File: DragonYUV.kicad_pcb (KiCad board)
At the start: 4 copper layers, 120 x 45.6 mm, 72 parts, among them IC1 74HCT273, IC11 74LS123N, IC2 MC6847, J1 Video Output, J2 Board Interconnect Male, J3 JTAG, J4 SVid, Q1 MMBT4401, Q2 NPN, Q3 NPN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

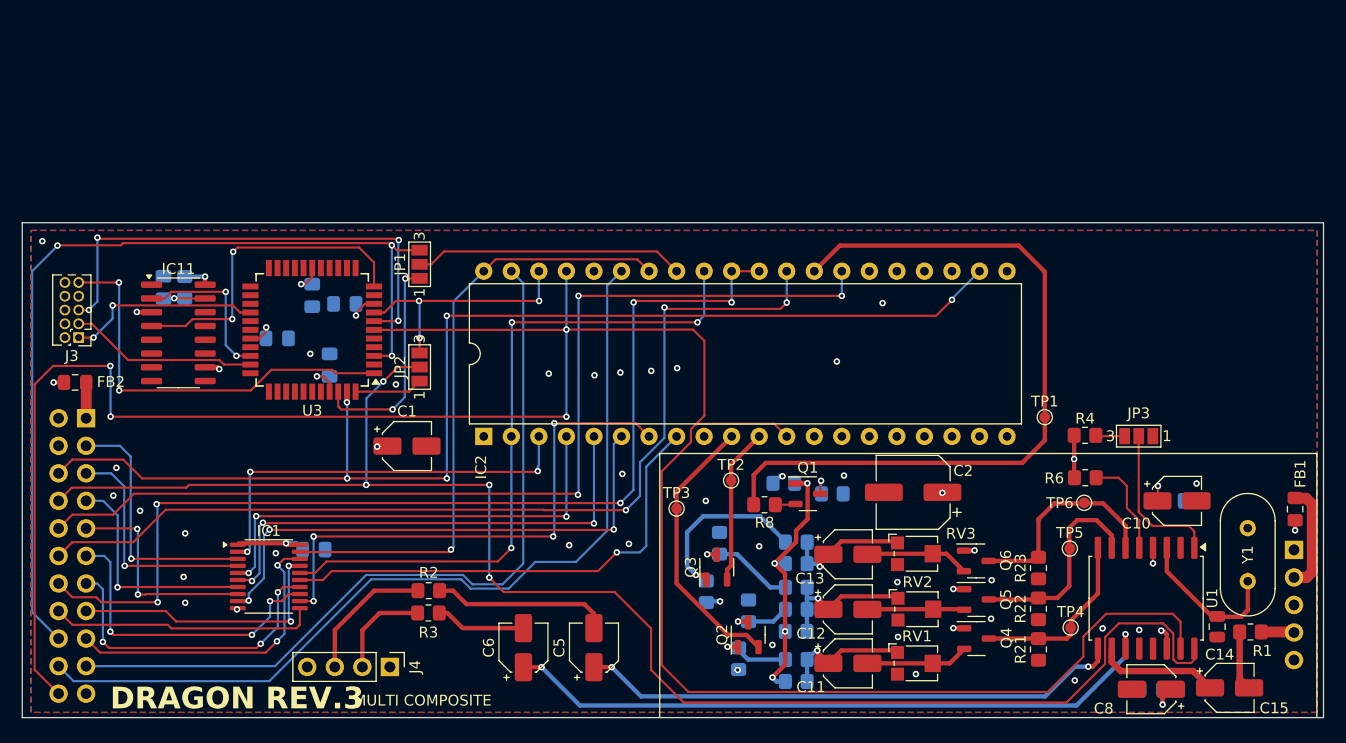
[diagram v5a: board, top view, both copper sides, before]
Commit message: rework schematics for demux of video
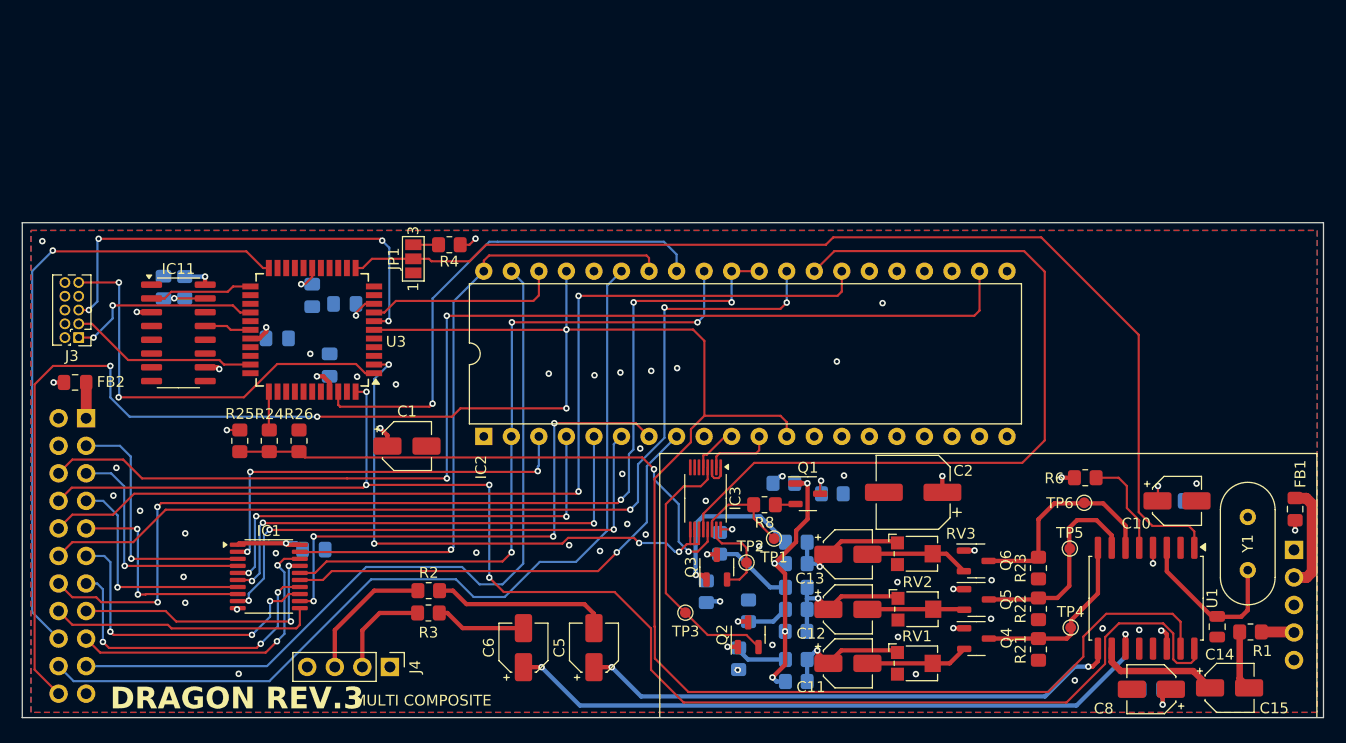
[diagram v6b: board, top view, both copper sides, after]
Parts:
- removed JP2: Video HS, Jumper:SolderJumper-3_P1.3mm_Open_Pad1.0x1.5mm_NumberLabels
- removed JP3: Video Format, Jumper:SolderJumper-3_P1.3mm_Open_Pad1.0x1.5mm_NumberLabels
- added IC3: MC14053, Package_SO:TSSOP-16_4.4x3.6mm_P0.4mm, F.Cu at (153.0, 106.9)
- added R24: 12K, Resistor_SMD:R_0805_2012Metric_Pad1.20x1.40mm_HandSolder, F.Cu at (112.8, 101.6)
- added R25: 8K2, Resistor_SMD:R_0805_2012Metric_Pad1.20x1.40mm_HandSolder, F.Cu at (110.1, 101.6)
- added R26: 1K8, Resistor_SMD:R_0805_2012Metric_Pad1.20x1.40mm_HandSolder, F.Cu at (115.5, 101.6)
- JP1: value Video Clock -> Video Format
- moved R4 61.2 mm to (129.4, 83.5), turned to 0 degrees
- moved TP1 27.4 mm to (159.4, 110.6)
- moved TP3 9.64 mm to (151.2, 117.4)
- moved TP2 7.70 mm to (156.8, 112.8)
- moved Y1 1.03 mm to (203.0, 108.6)
- moved JP1 0.77 mm to (126.1, 84.8)
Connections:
- IC11 pad 13: unconnected-(IC11A-Q-Pad13) -> SyncT
- IC11 pad 4: PhaseT -> unconnected-(IC11A-~{Q}-Pad4)
- IC2 pad 9: CHB -> unconnected-(IC2-CHB-Pad9)
- JP1 pad 1: CLK' -> GND
- JP1 pad 2: CLK -> Format
- JP1 pad 3: VCLK -> Net-(JP1-B)
- Q2 pad 2: phiB -> phiB'
- Q3 pad 2: phiA -> phiA'
- R4 pad 1: Net-(JP3-B) -> Net-(JP1-B)
- R8 pad 2: LUM -> LUM'
- TP1 pad 1: LUM -> LUM'
- TP2 pad 1: phiA -> phiA'
- TP3 pad 1: phiB -> phiB'
- U1 pad 1: Net-(JP3-C) -> Format
- U3 pad 11: PhaseT -> unconnected-(U3-I/O-Pad11)
- U3 pad 12: unconnected-(U3-I/O-Pad12) -> Format
- U3 pad 2: DA0' -> LUM CONTROL
- U3 pad 22: unconnected-(U3-I/O-Pad22) -> VCLK
- U3 pad 23: unconnected-(U3-I/O-Pad23) -> Burst
- U3 pad 28: unconnected-(U3-I/O-Pad28) -> SyncT
- U3 pad 3: VCLK -> unconnected-(U3-I/O-Pad3)
- U3 pad 30: CHROME CONTROL -> unconnected-(U3-I/O-Pad30)
- U3 pad 31: Burst -> unconnected-(U3-I/O-Pad31)
- U3 pad 33: LUM CONTROL -> unconnected-(U3-I/O-Pad33)
- U3 pad 34: PadLuma -> Net-(R24-Pad2)
- U3 pad 42: CLK' -> CLK
- U3 pad 43: DA0 -> unconnected-(U3-I/O-Pad43)
- U3 pad 44: ~{HS'} -> ~{NHS}
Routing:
- net Format: track 0.00 -> 101.1 mm
- net LUM CONTROL: track 0.00 -> 53.5 mm, vias 0 -> 4
- net PadLuma: track 0.00 -> 51.1 mm, vias 0 -> 2
- net PhaseT: track 29.9 -> 0.00 mm, vias 2 -> 0
- net VCLK: track 84.4 -> 58.2 mm, vias 3 -> 1
- net phiB': track 0.00 -> 24.7 mm
- net CLK: track 24.4 -> 46.5 mm, vias 0 -> 1
- net phiB: track 25.6 -> 4.44 mm
- net CLK': track 20.9 -> 0.00 mm, vias 2 -> 0
- net Net-(JP3-C): track 14.4 -> 0.00 mm
- net LUM': track 0.00 -> 9.15 mm
- net phiA': track 0.00 -> 8.27 mm
- net phiA: track 14.4 -> 6.47 mm
- net ~{HS'}: track 6.31 -> 0.00 mm
- net DA0: track 111.0 -> 105.0 mm, vias 5 -> 2
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
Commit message: compose verilog
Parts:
- removed C20: 330pF, Capacitor_SMD:C_0805_2012Metric_Pad1.18x1.45mm_HandSolder
- removed IC11: 74LS123N, Package_SO:SOIC-16_3.9x9.9mm_P1.27mm
- removed R5: 27K, Resistor_SMD:R_0805_2012Metric_Pad1.20x1.40mm_HandSolder
- removed TP4, TP6: TestPoint_Blue, TestPoint:TestPoint_Pad_D1.0mm
- removed TP5: TestPoint_Green, TestPoint:TestPoint_Pad_D1.0mm
- C16, C17, C18, C19, C3, C4, C7, R10, R11, R12, R13, R14, R15, R16, R17, R18, R19, R20, R7, R9: moved to F.Cu
- IC1: value 74HCT273 -> 74LS273; footprint Package_SO:TSSOP-20_4.4x6.5mm_P0.65mm -> Package_SO:SOIC-20W_7.5x12.8mm_P1.27mm
- IC3: footprint Package_SO:TSSOP-16_4.4x3.6mm_P0.4mm -> Package_SO:SOIC-16_3.9x9.9mm_P1.27mm
- J3: footprint Connector_PinHeader_1.27mm:PinHeader_2x05_P1.27mm_Vertical -> Connector_PinHeader_2.54mm:PinHeader_2x05_P2.54mm_Vertical
- R21, R22, R23: footprint Resistor_SMD:R_0805_2012Metric_Pad1.20x1.40mm_HandSolder -> Resistor_SMD:R_0603_1608Metric
- moved C2 33.9 mm to (206.0, 103.8), turned to -90 degrees
- moved C1 22.9 mm to (148.2, 99.0)
- moved IC2 20.9 mm to (153.4, 99.0)
- moved R9 20.9 mm to (144.7, 112.5), turned to 0 degrees
- moved TP1 19.9 mm to (139.6, 109.1)
- moved IC3 19.1 mm to (136.7, 116.7), turned to 0 degrees
- moved C8 18.7 mm to (186.8, 107.3), turned to 0 degrees
- moved C3 17.4 mm to (197.0, 107.3), turned to 0 degrees
- moved R7 15.6 mm to (144.7, 107.3)
- moved C7 14.9 mm to (181.3, 107.2), turned to 0 degrees
- moved C5 14.3 mm to (128.7, 117.7), turned to -90 degrees
- moved Q1 14.3 mm to (148.7, 110.5), turned to -90 degrees
- moved C14 14.1 mm to (191.9, 107.3), turned to 0 degrees
- moved R8 13.9 mm to (144.7, 109.3)
- moved TP2 13.2 mm to (143.7, 114.5), turned to 90 degrees
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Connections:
- IC1 pad 12: /Q4 -> /Q7
- IC1 pad 13: DO4 -> DO7
- IC1 pad 14: DO5 -> DO6
- IC1 pad 15: /Q5 -> /Q6
- IC1 pad 16: /Q6 -> /Q5
- IC1 pad 17: DO6 -> DO5
- IC1 pad 18: DO7 -> DO4
- IC1 pad 19: /Q7 -> /Q4
- IC3 pad 1: GND -> PadLuma
- IC3 pad 12: LUM -> phiA
- IC3 pad 13: PadLuma -> GND
- IC3 pad 14: LUM' -> phiA'
- IC3 pad 15: phiA' -> LUM'
- IC3 pad 2: phiA -> LUM
- U3 pad 23: Burst -> unconnected-(U3-I/O-Pad23)
- U3 pad 28: SyncT -> unconnected-(U3-I/O-Pad28)
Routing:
- net phiB: track 4.44 -> 60.8 mm
- net phiA: track 6.47 -> 59.4 mm
- net /Q6: track 63.6 -> 110.3 mm, vias 3 -> 5
- net ~{NHS}: track 139.0 -> 173.3 mm, vias 4 -> 7
- net /Q3: track 49.0 -> 80.3 mm, vias 3 -> 4
- net /Q5: track 43.3 -> 73.1 mm, vias 1 -> 2
- net +5V: track 53.0 -> 82.3 mm, vias 26 -> 20
- net /Q2: track 45.7 -> 73.8 mm, vias 3 -> 4
- net /Q7: track 58.7 -> 86.4 mm, vias 1 -> 5
- net /Q1: track 42.6 -> 69.7 mm, vias 3 -> 2
- net ~{A}/G: track 82.8 -> 109.4 mm, vias 0 -> 3
- net Net-(U1-CHROM_OUT): track 50.1 -> 76.4 mm, vias 2 -> 0
- net GM0: track 94.9 -> 120.8 mm
- net /Q0: track 38.2 -> 63.6 mm, vias 3 -> 2
- net GM1: track 88.9 -> 113.4 mm, vias 3 -> 5
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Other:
- board size 120 x 45.6 mm -> 120 x 46.3 mm
- board text added: "JP1 Video Format 1 = PAL 3 = NTSC"
- board text added: "Y1 must be correct for chosen format"
